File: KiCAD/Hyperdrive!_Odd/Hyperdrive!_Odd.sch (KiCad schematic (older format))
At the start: 65 parts, among them K1 ES1, K2 ES2, K3 ES3, K4 ES4, P1 H-Bridge PCB, P2 H-Bridge PCB, P3 Main Processor PCB, P4 MR, P5 ML, P6 Display PCB, P7 RIR PCB, SW1 SW_PUSH, SW2 SW_PUSH, SW3 SW_PUSH, SW4 SW_PUSH, U1 MAX14780, U10 TSOP4038, U2 QRE1113, U3 QRE1113, U4 MAX14780, U5 QRE1113, U6 QRE1113, U7 MCP6541, U8 QRE1113, U9 QRE1113

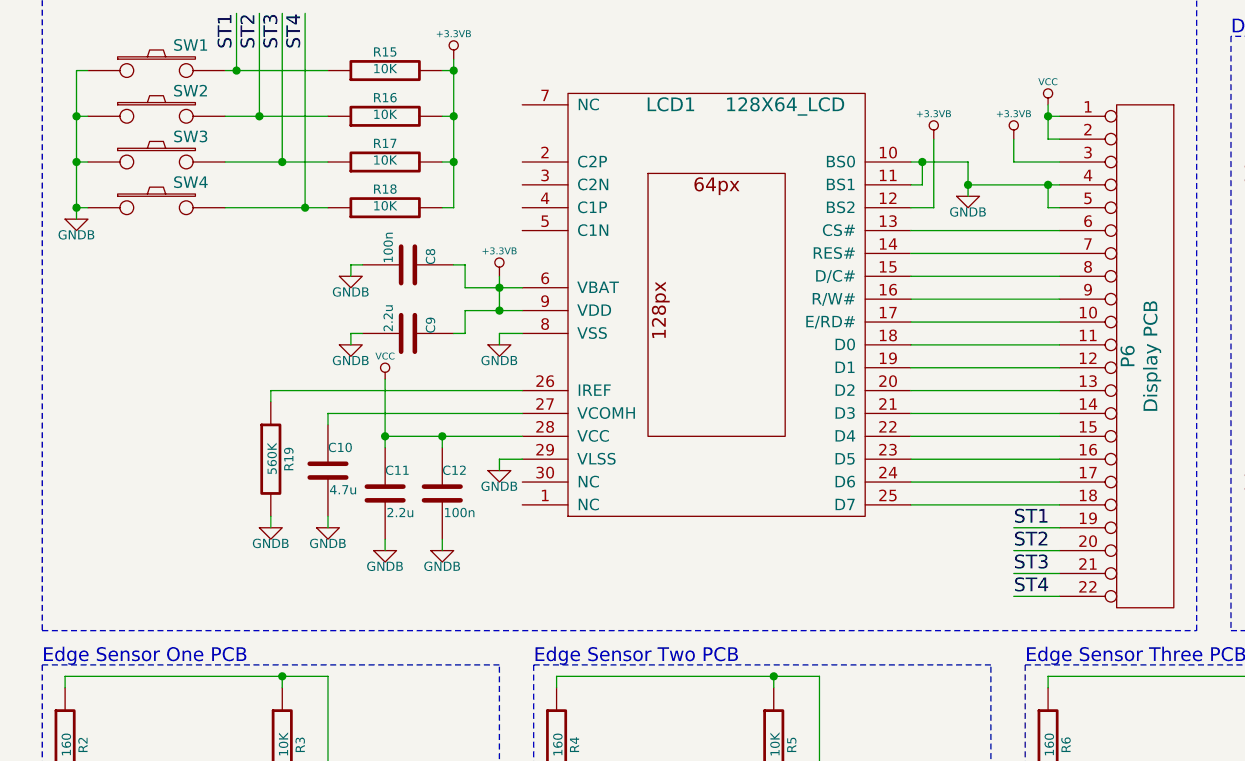
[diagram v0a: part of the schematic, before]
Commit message: Updated 3D-Model, and PCBs.
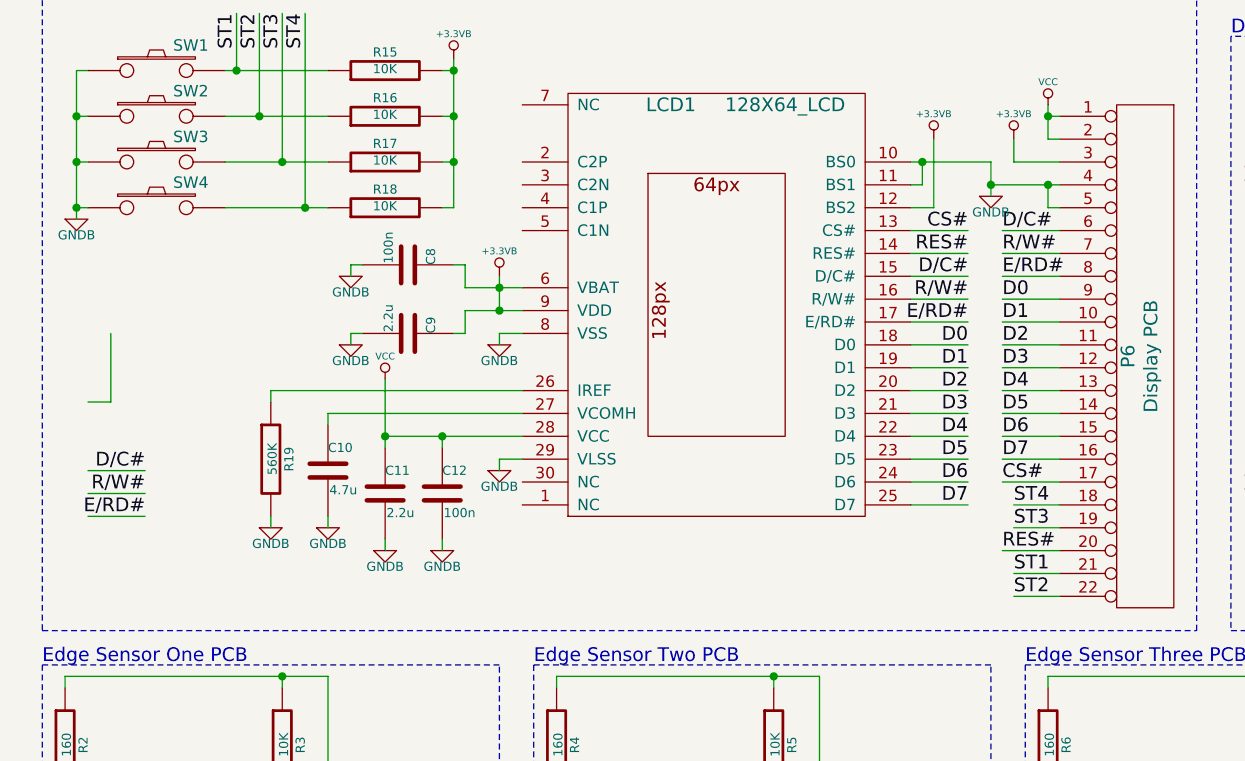
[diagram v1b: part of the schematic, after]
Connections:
- net labels added: CS#, D/C#, D0, D1, D2, D3, D4, D5, D6, D7, E/RD#, R/W#, RES#
- wire segments 299 -> 317
